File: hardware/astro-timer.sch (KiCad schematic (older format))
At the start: 21 parts, among them J1 AVR-ISP-6, J2 Conn_02x01, J3 Conn_01x05_Male, J4 Conn_02x01, SW1 SW_Push, SW2 SW_Push, SW3 SW_Push, U1 ATmega328P-PU, U2 LTV-817M, Y1 Crystal

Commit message: changing everything, nothing works yet
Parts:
- removed J2, J4: Conn_02x01, Connector_PinHeader_2.54mm:PinHeader_1x02_P2.54mm_Vertical, symbol Connector_Generic:Conn_02x01
- removed J3: Conn_01x05_Male, Connector_PinHeader_2.54mm:PinHeader_1x05_P2.54mm_Vertical, symbol Connector:Conn_01x05_Male
- removed SW1: SW_Push, Button_Switch_THT:SW_Tactile_Straight_KSA0Axx1LFTR, symbol Switch:SW_Push
- added BT1, BT2: Battery_Cell, Battery:BatteryHolder_Keystone_2460_1xAA, symbol Device:Battery_Cell
- added J1: Conn_01x02_Male, Connector_PinHeader_2.54mm:PinHeader_1x02_P2.54mm_Vertical, symbol Connector:Conn_01x02_Male
- added J3: SJ1-2503A, more_different_sj1:CUI_SJ1-2503A, symbol sj1-2503a:SJ1-2503A
- added SW1: SW_SPST, eg1218:EG1218, symbol Switch:SW_SPST
- added U3: EN11-HSM1AF15, en11:EN11HSM1AF15, symbol en11:EN11-HSM1AF15
- R9: footprint Resistor_THT:R_Axial_DIN0204_L3.6mm_D1.6mm_P2.54mm_Vertical -> Resistor_THT:R_Axial_DIN0204_L3.6mm_D1.6mm_P7.62mm_Horizontal
- renumbered J1 to J2, R8 to R1, R7 to R2, R6 to R3, R5 to R4, R4 to R5, R3 to R6, R2 to R7, R1 to R8
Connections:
- net labels added: a, b, c, d, dig1, dig2, dig3, dig4, dige, dp, e, enc_a, enc_b, enc_sw, f, g, pc, pc5, rst, sw1, sw2
- wire segments 86 -> 105
- no-connect marks 1 -> 3

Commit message: this is gonna be lit
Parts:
- BT1, BT2: footprint Battery:BatteryHolder_Keystone_2460_1xAA -> sparkfun-batteries:BATTERY-AAA
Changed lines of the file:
@@
 F 0 "BT1" H 3268 1696 50  0000 L CNN
 F 1 "Battery_Cell" H 3268 1605 50  0000 L CNN
-F 2 "Battery:BatteryHolder_Keystone_2460_1xAA" V 3150 1660 50  0001 C CNN
+F 2 "sparkfun-batteries:BATTERY-AAA" V 3150 1660 50  0001 C CNN
 F 3 "~" V 3150 1660 50  0001 C CNN
 	1    3150 1600
@@
 F 0 "BT2" H 3268 1996 50  0000 L CNN
 F 1 "Battery_Cell" H 3268 1905 50  0000 L CNN
-F 2 "Battery:BatteryHolder_Keystone_2460_1xAA" V 3150 1960 50  0001 C CNN
+F 2 "sparkfun-batteries:BATTERY-AAA" V 3150 1960 50  0001 C CNN
 F 3 "~" V 3150 1960 50  0001 C CNN
 	1    3150 1900

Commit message: creeping toward a layout
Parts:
- BT1, BT2: symbol Device:Battery_Cell -> sparkfun-batts:BATTERY-AAA
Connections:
- net GND: now also BT2.GND@ (-); no longer BT2.2 (-)
- net at SW1.1 (A): now also BT1.PWR@ (+); no longer BT1.1 (+)
- new net: BT1.GND@ (-), BT2.PWR@ (+)
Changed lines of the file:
@@
 L power:GND #PWR01
 U 1 1 60349228
-P 3150 2000
-F 0 "#PWR01" H 3150 1750 50  0001 C CNN
-F 1 "GND" H 3155 1827 50  0000 C CNN
-F 2 "" H 3150 2000 50  0001 C CNN
-F 3 "" H 3150 2000 50  0001 C CNN
-	1    3150 2000
+P 3150 2200
+F 0 "#PWR01" H 3150 1950 50  0001 C CNN
+F 1 "GND" H 3155 2027 50  0000 C CNN
+F 2 "" H 3150 2200 50  0001 C CNN
+F 3 "" H 3150 2200 50  0001 C CNN
+	1    3150 2200
 	1    0    0    -1
 $EndComp
@@
 $EndComp
 $Comp
-L Device:Battery_Cell BT1
+L sparkfun-batts:BATTERY-AAA BT1
 U 1 1 603EB8A6
 P 3150 1600
@@
 F 3 "~" V 3150 1660 50  0001 C CNN
 	1    3150 1600
-	1    0    0    -1
+	0    1    1    0
 $EndComp
 $Comp
-L Device:Battery_Cell BT2
+L sparkfun-batts:BATTERY-AAA BT2
 U 1 1 603EBBDC
-P 3150 1900
-F 0 "BT2" H 3268 1996 50  0000 L CNN
-F 1 "Battery_Cell" H 3268 1905 50  0000 L CNN
-F 2 "sparkfun-batteries:BATTERY-AAA" V 3150 1960 50  0001 C CNN
-F 3 "~" V 3150 1960 50  0001 C CNN
-	1    3150 1900
-	1    0    0    -1
+P 3150 2000
+F 0 "BT2" H 3268 2096 50  0000 L CNN
+F 1 "Battery_Cell" H 3268 2005 50  0000 L CNN
+F 2 "sparkfun-batteries:BATTERY-AAA" V 3150 2060 50  0001 C CNN
+F 3 "~" V 3150 2060 50  0001 C CNN
+	1    3150 2000
+	0    1    1    0
 $EndComp
 Wire Wire Line

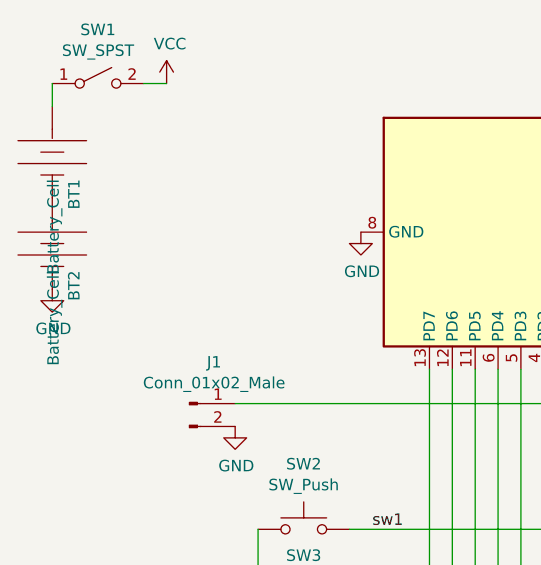
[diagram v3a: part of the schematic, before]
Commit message: improved battery layout
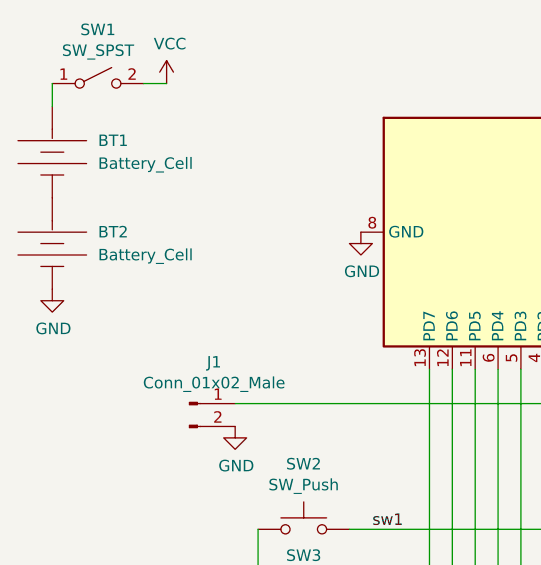
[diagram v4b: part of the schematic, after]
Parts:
- renumbered BT2 to BT1, BT1 to BT2
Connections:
- net GND: now also BT2.GND@ (-); no longer BT1.GND@ (-)
- net at SW1.1 (A): now also BT1.PWR@ (+); no longer BT2.PWR@ (+)
- new net: BT1.GND@ (-), BT2.PWR@ (+)
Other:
- moved on the sheet: BT1, BT2
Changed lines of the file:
@@
+$EndComp
+$Comp
+L sparkfun-batts:BATTERY-AAA BT2
+U 1 1 603EB8A6
+P 3150 2000
+F 0 "BT2" V 3100 2200 50  0000 L CNN
+F 1 "Battery_Cell" V 3200 2200 50  0000 L CNN
+F 2 "sparkfun-batteries:BATTERY-AAA" V 3150 2060 50  0001 C CNN
+F 3 "~" V 3150 2060 50  0001 C CNN
+	1    3150 2000
+	0    1    1    0
 $EndComp
 $Comp
 L sparkfun-batts:BATTERY-AAA BT1
-U 1 1 603EB8A6
+U 1 1 603EBBDC
 P 3150 1600
-F 0 "BT1" H 3268 1696 50  0000 L CNN
-F 1 "Battery_Cell" H 3268 1605 50  0000 L CNN
+F 0 "BT1" V 3100 1800 50  0000 L CNN
+F 1 "Battery_Cell" V 3200 1800 50  0000 L CNN
 F 2 "sparkfun-batteries:BATTERY-AAA" V 3150 1660 50  0001 C CNN
 F 3 "~" V 3150 1660 50  0001 C CNN
@@
 	0    1    1    0
 $EndComp
-$Comp
-L sparkfun-batts:BATTERY-AAA BT2
-U 1 1 603EBBDC
-P 3150 2000
-F 0 "BT2" H 3268 2096 50  0000 L CNN
-F 1 "Battery_Cell" H 3268 2005 50  0000 L CNN
-F 2 "sparkfun-batteries:BATTERY-AAA" V 3150 2060 50  0001 C CNN
-F 3 "~" V 3150 2060 50  0001 C CNN
-	1    3150 2000
-	0    1    1    0
-$EndComp

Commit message: moar pcb tweaks
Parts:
- removed J3: SJ1-2503A, more_different_sj1:CUI_SJ1-2503A, symbol sj1-2503a:SJ1-2503A
- removed U3: EN11-HSM1AF15, en11:EN11HSM1AF15, symbol en11:EN11-HSM1AF15
- added J3: AudioJack2, more_different_sj1:CUI_SJ1-2503A, symbol Connector:AudioJack2
- added SW4: Rotary_Encoder_Switch, en11:EN11HSM1AF15, symbol Device:Rotary_Encoder_Switch
- SW1: footprint eg1218:EG1218 -> digikey:Switch_Slide_11.6x4mm_EG1218
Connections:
- net GND: now also SW4.C, SW4.S2
- net enc_a: now also SW4.A
- net enc_b: now also SW4.B
- net enc_sw: now also SW4.S1
- net at U2.3: now also J3.S
- net at U2.4: now also J3.T
- no-connect marks 3 -> 1
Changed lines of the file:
@@
 L power:GND #PWR012
 U 1 1 60408112
-P 9550 3000
-F 0 "#PWR012" H 9550 2750 50  0001 C CNN
-F 1 "GND" H 9555 2827 50  0000 C CNN
-F 2 "" H 9550 3000 50  0001 C CNN
-F 3 "" H 9550 3000 50  0001 C CNN
-	1    9550 3000
+P 9150 3050
+F 0 "#PWR012" H 9150 2800 50  0001 C CNN
+F 1 "GND" H 9155 2877 50  0000 C CNN
+F 2 "" H 9150 3050 50  0001 C CNN
+F 3 "" H 9150 3050 50  0001 C CNN
+	1    9150 3050
 	1    0    0    -1
 $EndComp
@@
 F 0 "SW1" H 3350 1535 50  0000 C CNN
 F 1 "SW_SPST" H 3350 1444 50  0000 C CNN
-F 2 "eg1218:EG1218" H 3350 1300 50  0001 C CNN
+F 2 "digikey:Switch_Slide_11.6x4mm_EG1218" H 3350 1300 50  0001 C CNN
 F 3 "~" H 3350 1300 50  0001 C CNN
 	1    3350 1300
@@
 Wire Wire Line
 	3550 1300 3650 1300
-$Comp
-L sj1-2503a:SJ1-2503A J3
-U 1 1 60401D7D
-P 8550 5600
-F 0 "J3" H 8320 5604 50  0000 R CNN
-F 1 "SJ1-2503A" H 8320 5695 50  0000 R CNN
-F 2 "more_different_sj1:CUI_SJ1-2503A" H 8550 5600 50  0001 L BNN
-F 3 "" H 8550 5600 50  0001 L BNN
-F 4 "B" H 8550 5600 50  0001 L BNN "REV"
-F 5 "Manufacturer Recommendation" H 8550 5600 50  0001 L BNN "STANDARD"
-F 6 "CUI INC" H 8550 5600 50  0001 L BNN "MANUFACTURER"
-	1    8550 5600
-	-1   0    0    1
-$EndComp
-$Comp
-L en11:EN11-HSM1AF15 U3
-U 1 1 6040D732
-P 9050 2300
-F 0 "U3" V 8869 2300 50  0000 C CNN
-F 1 "EN11-HSM1AF15" V 8960 2300 50  0000 C CNN
-F 2 "en11:EN11HSM1AF15" H 9900 2600 50  0001 L CNN
-F 3 "http://www.mouser.com/datasheet/2/414/Datasheet_RotaryEncoder_EN11Series-1154703.pdf" H 9900 2500 50  0001 L CNN
-F 4 "BI TECHNOLOGIES / TT ELECTRONICS - EN11-HSM1AF15 - INCREMENTAL ENCODER" H 9900 2400 50  0001 L CNN "Description"
-F 5 "22.1" H 9900 2300 50  0001 L CNN "Height"
-F 6 "BI Technologies" H 9900 2200 50  0001 L CNN "Manufacturer_Name"
-F 7 "EN11-HSM1AF15" H 9900 2100 50  0001 L CNN "Manufacturer_Part_Number"
-F 8 "858-EN11-HSM1AF15" H 9900 2000 50  0001 L CNN "Mouser Part Number"
-F 9 "https://www.mouser.co.uk/ProductDetail/BI-Technologies-TT-Electronics/EN11-HSM1AF15/?qs=u1MaZ2%2F4xgsleMatSs8Sqg%3D%3D" H 9900 1900 50  0001 L CNN "Mouser Price/Stock"
-F 10 "EN11-HSM1AF15" H 9900 1800 50  0001 L CNN "Arrow Part Number"
-F 11 "https://www.arrow.com/en/products/en11-hsm1af15/bi-technologies" H 9900 1700 50  0001 L CNN "Arrow Price/Stock"
-	1    9050 2300
-	0    1    1    0
-$EndComp
 Wire Wire Line
-	9550 2700 9950 2700
+	9150 2700 9400 2700
 Wire Wire Line
-	9950 2700 9950 3500
+	9400 2700 9400 3500
 Wire Wire Line
-	9950 3500 7800 3500
+	9400 3500 7800 3500
 Wire Wire Line
 	7800 3500 7800 3250
@@
 	8450 2800 8450 3000
 Wire Wire Line
-	9550 2800 9550 3000
-NoConn ~ 9050 3300
-NoConn ~ 9050 2300
-Wire Wire Line
-	7900 5700 8000 5700
-Wire Wire Line
-	7800 5800 7950 5800
-Wire Wire Line
-	8150 5500 7950 5500
-Wire Wire Line
-	7950 5500 7950 5800
-Connection ~ 7950 5800
-Wire Wire Line
-	7950 5800 8150 5800
-Wire Wire Line
-	8150 5600 8000 5600
-Wire Wire Line
-	8000 5600 8000 5700
-Connection ~ 8000 5700
-Wire Wire Line
-	8000 5700 8150 5700
+	9150 2900 9150 3050
 $Comp
 L Connector:Conn_01x02_Male J1
@@
 Wire Wire Line
 	5800 2700 5800 2550
+$Comp
+L Connector:AudioJack2 J3
+U 1 1 603FA50D
+P 8350 5700
+F 0 "J3" H 8170 5683 50  0000 R CNN
+F 1 "AudioJack2" H 8170 5774 50  0000 R CNN
+F 2 "more_different_sj1:CUI_SJ1-2503A" H 8350 5700 50  0001 C CNN
+F 3 "~" H 8350 5700 50  0001 C CNN
+	1    8350 5700
+	-1   0    0    1
+$EndComp
+Wire Wire Line
+	7800 5800 8150 5800
+Wire Wire Line
+	7900 5700 8150 5700
+$Comp
+L Device:Rotary_Encoder_Switch SW4
+U 1 1 6041992A
+P 8850 2800
+F 0 "SW4" H 8850 3167 50  0000 C CNN
+F 1 "Rotary_Encoder_Switch" H 8850 3076 50  0000 C CNN
+F 2 "en11:EN11HSM1AF15" H 8700 2960 50  0001 C CNN
+F 3 "~" H 8850 3060 50  0001 C CNN
+	1    8850 2800
+	1    0    0    -1
+$EndComp
 $EndSCHEMATC

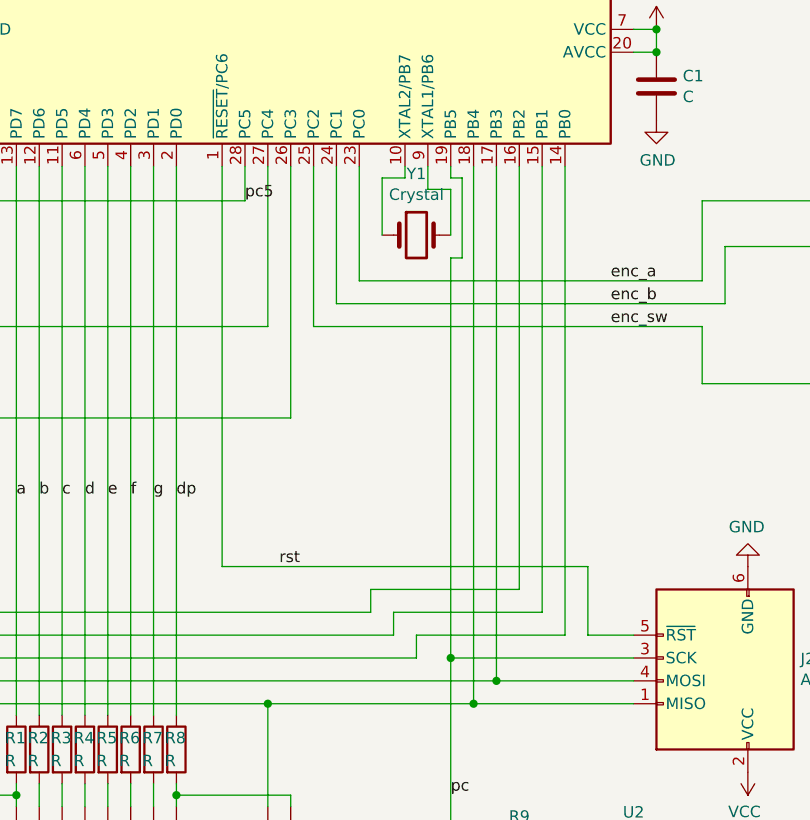
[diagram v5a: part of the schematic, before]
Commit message: add crystal caps
and do a bit of odd routing to put a ground plane under
the crystal, while we're at it

the prior version of this device worked fine without either
of these things, but the datasheet asks for both, and since
I'm revising the board anyway
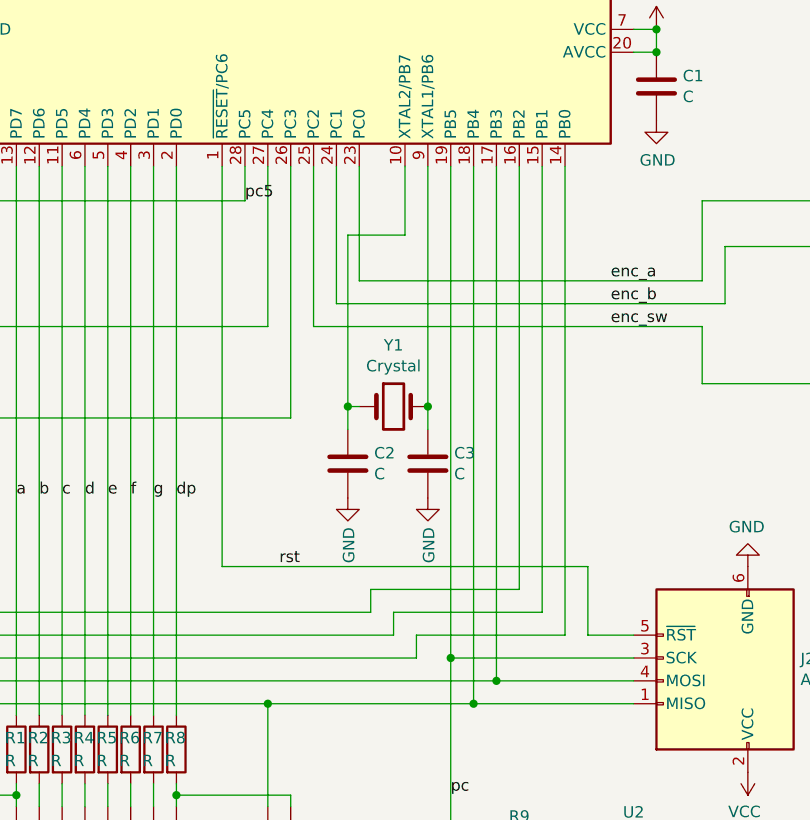
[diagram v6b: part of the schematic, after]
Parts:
- added C2, C3: C, Capacitor_THT:C_Disc_D3.0mm_W2.0mm_P2.50mm, symbol Device:C
- C1: footprint Capacitor_THT:C_Disc_D3.0mm_W2.0mm_P2.50mm -> Capacitor_THT:C_Disc_D3.0mm_W1.6mm_P2.50mm
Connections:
- net GND: now also C2.2, C3.2
- net at U1.10 (XTAL2/PB7), Y1.1: now also C2.1
- net at U1.9 (XTAL1/PB6), Y1.2: now also C3.1
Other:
- moved on the sheet: Y1
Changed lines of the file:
@@
 	3900 4800 3900 5350
-$Comp
-L Device:Crystal Y1
-U 1 1 603212E8
-P 6550 2850
-F 0 "Y1" H 6550 3118 50  0000 C CNN
-F 1 "Crystal" H 6550 3027 50  0000 C CNN
-F 2 "Crystal:Crystal_Round_D2.0mm_Vertical" H 6550 2850 50  0001 C CNN
-F 3 "~" H 6550 2850 50  0001 C CNN
-	1    6550 2850
-	1    0    0    -1
-$EndComp
 $Comp
 L Connector:AVR-ISP-6 J2
@@
 F 0 "C1" H 7715 2246 50  0000 L CNN
 F 1 "C" H 7715 2155 50  0000 L CNN
-F 2 "Capacitor_THT:C_Disc_D3.0mm_W2.0mm_P2.50mm" H 7638 2050 50  0001 C CNN
+F 2 "Capacitor_THT:C_Disc_D3.0mm_W1.6mm_P2.50mm" H 7638 2050 50  0001 C CNN
 F 3 "~" H 7600 2200 50  0001 C CNN
 	1    7600 2200
@@
 Wire Wire Line
 	6800 2550 6800 4900
-Wire Wire Line
-	6500 2550 6500 2600
-Wire Wire Line
-	6500 2600 6400 2600
-Wire Wire Line
-	6600 2550 6600 2650
-Wire Wire Line
-	6600 2650 6700 2650
-Wire Wire Line
-	6400 2600 6400 2850
-Wire Wire Line
-	6700 2650 6700 2850
-Wire Wire Line
-	6700 2950 6750 2950
-Wire Wire Line
-	6750 2950 6750 2600
-Wire Wire Line
-	6750 2600 6700 2600
-Wire Wire Line
-	6700 2600 6700 2550
-Wire Wire Line
-	6700 2950 6700 4700
 Wire Wire Line
 	4050 3650 4050 3250
@@
 	1    0    0    -1
 $EndComp
+$Comp
+L Device:Crystal Y1
+U 1 1 603212E8
+P 6450 3600
+F 0 "Y1" H 6450 3868 50  0000 C CNN
+F 1 "Crystal" H 6450 3777 50  0000 C CNN
+F 2 "Crystal:Crystal_Round_D2.0mm_Vertical" H 6450 3600 50  0001 C CNN
+F 3 "~" H 6450 3600 50  0001 C CNN
+	1    6450 3600
+	1    0    0    -1
+$EndComp
+Wire Wire Line
+	6500 2550 6500 2850
+Wire Wire Line
+	6700 2550 6700 4700
+Wire Wire Line
+	6500 2850 6250 2850
+Wire Wire Line
+	6250 2850 6250 3600
+Wire Wire Line
+	6600 2550 6600 3600
+Wire Wire Line
+	6300 3600 6250 3600
+Wire Wire Line
+	6250 3600 6250 3700
+Connection ~ 6250 3600
+Wire Wire Line
+	6600 3600 6600 3700
+Connection ~ 6600 3600
+$Comp
+L Device:C C2
+U 1 1 6041BDCC
+P 6250 3850
+F 0 "C2" H 6365 3896 50  0000 L CNN
+F 1 "C" H 6365 3805 50  0000 L CNN
+F 2 "Capacitor_THT:C_Disc_D3.0mm_W2.0mm_P2.50mm" H 6288 3700 50  0001 C CNN
+F 3 "~" H 6250 3850 50  0001 C CNN
+	1    6250 3850
+	1    0    0    -1
+$EndComp
+$Comp
+L Device:C C3
+U 1 1 6041C3F5
+P 6600 3850
+F 0 "C3" H 6715 3896 50  0000 L CNN
+F 1 "C" H 6715 3805 50  0000 L CNN
+F 2 "Capacitor_THT:C_Disc_D3.0mm_W2.0mm_P2.50mm" H 6638 3700 50  0001 C CNN
+F 3 "~" H 6600 3850 50  0001 C CNN
+	1    6600 3850
+	1    0    0    -1
+$EndComp
+$Comp
+L power:GND #PWR0101
+U 1 1 6041CA29
+P 6250 4000
+F 0 "#PWR0101" H 6250 3750 50  0001 C CNN
+F 1 "GND" V 6255 3872 50  0000 R CNN
+F 2 "" H 6250 4000 50  0001 C CNN
+F 3 "" H 6250 4000 50  0001 C CNN
+	1    6250 4000
+	1    0    0    -1
+$EndComp
+$Comp
+L power:GND #PWR0102
+U 1 1 6041D3F2
+P 6600 4000
+F 0 "#PWR0102" H 6600 3750 50  0001 C CNN
+F 1 "GND" V 6605 3872 50  0000 R CNN
+F 2 "" H 6600 4000 50  0001 C CNN
+F 3 "" H 6600 4000 50  0001 C CNN
+	1    6600 4000
+	1    0    0    -1
+$EndComp

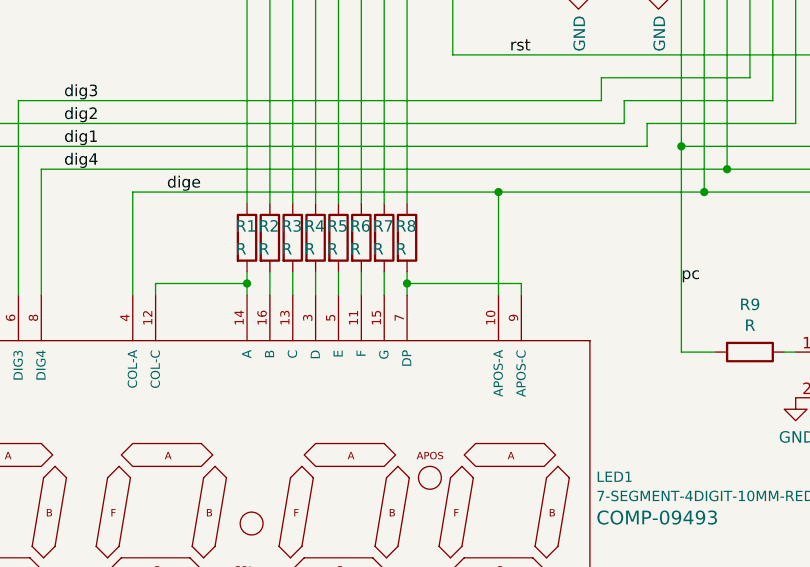
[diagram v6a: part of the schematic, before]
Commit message: plex apostrophe with C segment
because why not, that's how Lite-On does it

also tweak the ground plane keepouts under the battery clips
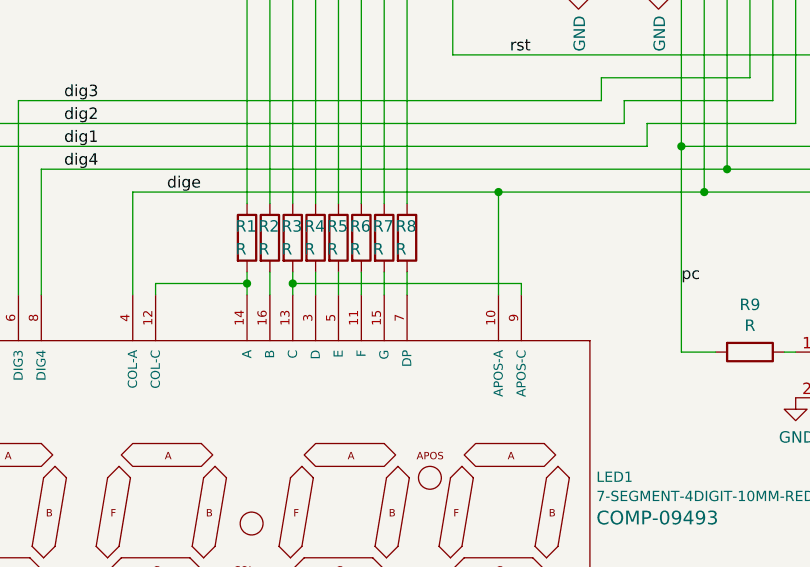
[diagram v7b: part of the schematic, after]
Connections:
- net at LED1.13 (C), R3.2: now also LED1.9 (APOS-C)
- net at LED1.7 (DP), R8.2: no longer LED1.9 (APOS-C)
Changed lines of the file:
@@
 	6850 5600 6700 5600
 Wire Wire Line
-	5500 5250 5500 5300
-Wire Wire Line
 	5400 5250 5400 5350
 Wire Wire Line
@@
 	5100 5250 5100 5350
 Wire Wire Line
-	5000 5250 5000 5350
+	5000 5250 5000 5300
 Wire Wire Line
 	4900 5250 4900 5350
@@
 Wire Wire Line
 	4800 5300 4800 5350
-Wire Wire Line
-	5500 5300 6000 5300
-Connection ~ 5500 5300
-Wire Wire Line
-	5500 5300 5500 5350
 Wire Wire Line
 	4300 4900 5900 4900
@@
 	1    0    0    -1
 $EndComp
+Wire Wire Line
+	5500 5250 5500 5350
+Wire Wire Line
+	6000 5300 5000 5300
+Connection ~ 5000 5300
+Wire Wire Line
+	5000 5300 5000 5350
 $EndSCHEMATC
